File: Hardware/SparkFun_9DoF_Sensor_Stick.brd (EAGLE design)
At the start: 34.3 x 10.2 mm, 32 parts, among them U1 ITG-32001:1, U2 ADXL345", U3 3.3V/150mA, U4 HMC5883LSMD

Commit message: Updating for QC checks
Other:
- board text added: "PCB Thickness: 0.036 inches"
- board text added: "PWR"
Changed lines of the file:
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@@
 <setting verticaltext="up"/>
 </settings>
-<grid distance="0.01" unitdist="inch" unit="inch" style="lines" multiple="1" display="yes" altdistance="0.005" altunitdist="inch" altunit="inch"/>
+<grid distance="0.02" unitdist="inch" unit="inch" style="lines" multiple="1" display="yes" altdistance="0.005" altunitdist="inch" altunit="inch"/>
 <layers>
 <layer number="1" name="Top" color="4" fill="1" visible="yes" active="yes"/>
@@
 <layer number="45" name="Holes" color="7" fill="1" visible="yes" active="yes"/>
 <layer number="46" name="Milling" color="3" fill="1" visible="no" active="yes"/>
-<layer number="47" name="Measures" color="7" fill="1" visible="yes" active="yes"/>
+<layer number="47" name="Measures" color="7" fill="1" visible="no" active="yes"/>
 <layer number="48" name="Document" color="7" fill="1" visible="no" active="yes"/>
 <layer number="49" name="Reference" color="7" fill="1" visible="yes" active="yes"/>
@@
 <text x="18.288" y="6.35" size="0.8128" layer="22" font="vector" ratio="15" rot="MR0">GYRO</text>
 <text x="7.874" y="11.176" size="1.778" layer="47" font="vector" ratio="15">Units in inches</text>
+<text x="7.62" y="13.97" size="1.778" layer="51" font="vector" ratio="15">PCB Thickness: 0.036 inches</text>
+<text x="7.239" y="6.477" size="0.8128" layer="21" font="vector" ratio="15" rot="R90">PWR</text>
 </plain>
 <attributes>

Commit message: Changes from engineering review
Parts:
- removed SJ2: JUMPER-PAD-2-NC_BY_TRACE, SparkFun-Passives:PAD-JUMPER-2-NC_BY_TRACE_YES_SILK
- added R4, R5: DNP, SparkFun-Resistors:0603-RES
- added SJ5: JUMPER-PAD-3-2OF3_NC_BY_TRACE_LARGE, SparkFun-Passives:PAD-JUMPER-3-2OF3_NC_BY_TRACE_YES_SILK_LARGE
- SJ3: value JUMPER-PAD-2-NC_BY_TRACE -> JUMPER-PAD-3-2OF3_NC_BY_TRACE_LARGE; device SparkFun-Passives:PAD-JUMPER-2-NC_BY_TRACE_YES_SILK -> SparkFun-Passives:PAD-JUMPER-3-2OF3_NC_BY_TRACE_YES_SILK_LARGE
- moved U$3 1.15 mm to (7.33, 1.62)
- moved SJ3 0.76 mm to (17.9, 5.08)
- moved R3 0.13 mm to (8.74, 8.51)
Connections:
- new net N$11: R4.1, SJ3.1
- new net N$13: R5.1, SJ5.1
- net 3.3V: now also R4.2, R5.2
- net GND: now also SJ3.3, SJ5.3; no longer SJ2.1, SJ3.1
- net N$10: now also SJ5.2; no longer SJ2.2
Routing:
- net SCL: track 48.2 -> 42.0 mm
- net 3.3V: track 67.8 -> 71.6 mm, vias 5 -> 7
- net N$10: track 5.16 -> 8.01 mm
- net SDA: track 40.5 -> 42.9 mm
- net N$9: track 3.89 -> 5.76 mm
- net N$13: track 0.00 -> 1.54 mm
- net N$11: track 0.00 -> 1.54 mm
- net GND: track 17.4 -> 18.1 mm
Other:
- board text added: "GYRO ADD."
- board text added: "MAG."
- board text removed: "MAGNETO"

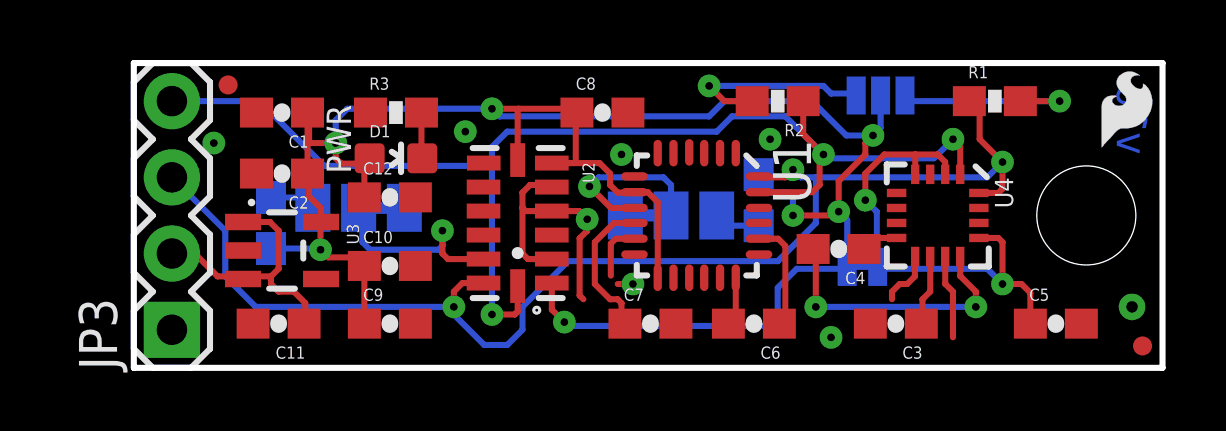
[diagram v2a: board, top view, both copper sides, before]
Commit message: Fixing QC issues
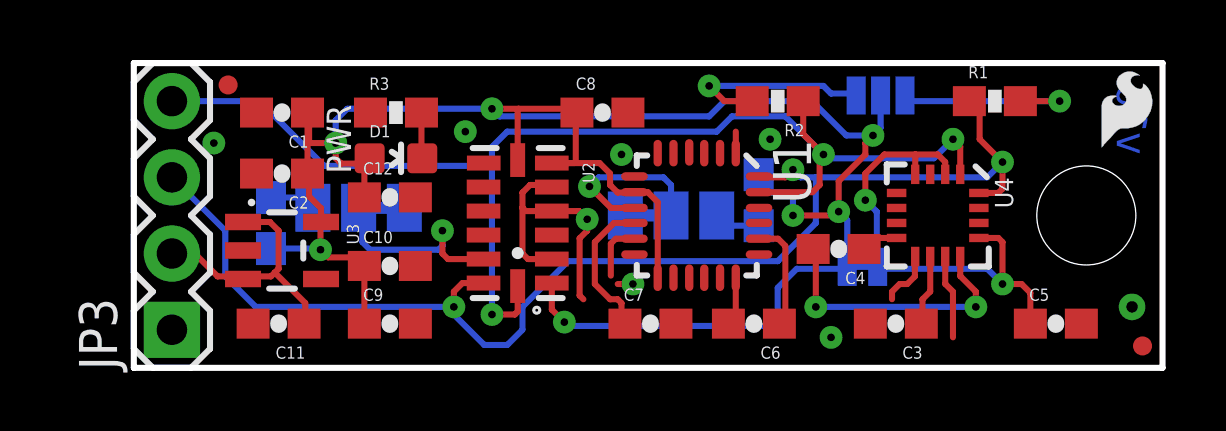
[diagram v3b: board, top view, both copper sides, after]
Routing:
- net GND: track 18.1 -> 18.8 mm
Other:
- board text added: "ADDR"
- board text added: "GYRO ADDR"
- board text removed: "ACL"
- board text removed: "ADD."
- board text removed: "GYRO ADD."
- board text removed: "MAG."
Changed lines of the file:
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@@
 <setting verticaltext="up"/>
 </settings>
-<grid distance="0.05" unitdist="inch" unit="inch" style="lines" multiple="1" display="yes" altdistance="0.005" altunitdist="inch" altunit="inch"/>
+<grid distance="0.005" unitdist="inch" unit="inch" style="lines" multiple="1" display="yes" altdistance="0.005" altunitdist="inch" altunit="inch"/>
 <layers>
 <layer number="1" name="Top" color="4" fill="1" visible="yes" active="yes"/>
@@
 <circle x="12.03325" y="2.88925" radius="0.635" width="0.2032" layer="22"/>
 <circle x="31.75" y="5.08" radius="1.27" width="0.254" layer="49"/>
-<text x="4.699" y="0.889" size="0.8128" layer="22" font="vector" ratio="15" rot="MR0">GND</text>
-<text x="4.699" y="3.429" size="0.8128" layer="22" font="vector" ratio="15" rot="MR0">VCC</text>
-<text x="4.699" y="5.969" size="0.8128" layer="22" font="vector" ratio="15" rot="MR0">SDA</text>
-<text x="4.445" y="8.509" size="0.8128" layer="22" font="vector" ratio="15" rot="MR0">SCL</text>
+<text x="3.429" y="2.413" size="0.8128" layer="22" font="vector" ratio="15" rot="MR270">GND</text>
+<text x="3.429" y="4.953" size="0.8128" layer="22" font="vector" ratio="15" rot="MR270">VCC</text>
+<text x="3.429" y="7.493" size="0.8128" layer="22" font="vector" ratio="15" rot="MR270">SDA</text>
+<text x="3.429" y="10.033" size="0.8128" layer="22" font="vector" ratio="15" rot="MR270">SCL</text>
 <text x="17.526" y="8.41375" size="1.4224" layer="22" font="vector" ratio="15" rot="MR0">9DOF Stick</text>
 <text x="13.68425" y="0.73025" size="1.016" layer="22" font="vector" ratio="15" rot="MR0">X</text>
@@
 <text x="14.57325" y="5.17525" size="1.016" layer="22" font="vector" ratio="15" rot="MR0">ACCEL</text>
 <text x="20.09775" y="0.254" size="1.016" layer="22" font="vector" ratio="15" rot="MR90">GYRO</text>
-<text x="29.2735" y="4.5085" size="1.016" layer="22" font="vector" ratio="15" rot="MR0">MAG.</text>
+<text x="29.2735" y="4.5085" size="1.016" layer="22" font="vector" ratio="15" rot="MR0">MAG</text>
 <text x="26.67" y="-12.7" size="1.778" layer="51" font="vector" ratio="15">C. Taylor and N. Seidle</text>
 <text x="32.766" y="7.112" size="1.016" layer="16" font="vector" ratio="20" rot="MR90">v16</text>
@@
 <text x="23.114" y="8.636" size="0.8128" layer="22" font="vector" ratio="15" rot="MR0">P/U</text>
 <text x="25.273" y="4.572" size="0.8128" layer="22" font="vector" ratio="15" rot="MR0">MAG</text>
-<text x="25.4" y="1.397" size="0.8128" layer="22" font="vector" ratio="15" rot="MR0">ADD.</text>
-<text x="8.636" y="3.302" size="0.8128" layer="22" font="vector" ratio="15" rot="MR0">ADD.</text>
-<text x="8.636" y="6.477" size="0.8128" layer="22" font="vector" ratio="15" rot="MR0">ACL</text>
-<text x="21.082" y="6.223" size="0.8128" layer="22" font="vector" ratio="15" rot="MR0">GYRO ADD.</text>
+<text x="25.654" y="1.397" size="0.8128" layer="22" font="vector" ratio="15" rot="MR0">ADDR</text>
+<text x="9.398" y="3.302" size="0.8128" layer="22" font="vector" ratio="15" rot="MR0">ADDR</text>
+<text x="9.398" y="6.477" size="0.8128" layer="22" font="vector" ratio="15" rot="MR0">ACCEL</text>
+<text x="19.304" y="6.223" size="0.8128" layer="22" font="vector" ratio="15" rot="MR0">GYRO
+ADDR</text>
 <text x="6.223" y="-6.223" size="1.778" layer="47" font="vector" ratio="15">Units in inches</text>
 <text x="-2.54" y="13.335" size="1.778" layer="51" font="vector" ratio="15">PCB Thickness: 0.036 inches</text>
@@
 <wire x1="15.113" y1="4.953" x2="15.113" y2="4.572" width="0.2032" layer="1"/>
 <wire x1="15.113" y1="4.572" x2="14.859" y2="4.318" width="0.2032" layer="1"/>
+<wire x1="20.066" y1="7.493" x2="20.066" y2="7.874" width="0.2032" layer="1"/>
+<wire x1="20.06505" y1="7.1562" x2="20.06505" y2="7.49205" width="0.2032" layer="1"/>
+<wire x1="20.06505" y1="7.49205" x2="20.066" y2="7.493" width="0.2032" layer="1"/>
 </signal>
 <signal name="SDA">
@@
 <wire x1="4.5364" y1="4.8616" x2="4.826" y2="4.572" width="0.2032" layer="1"/>
 <wire x1="4.826" y1="4.572" x2="4.826" y2="3.302" width="0.2032" layer="1"/>
-<wire x1="4.826" y1="3.302" x2="4.572" y2="3.048" width="0.2032" layer="1"/>
+<wire x1="4.826" y1="3.302" x2="4.699" y2="3.175" width="0.2032" layer="1"/>
+<wire x1="4.699" y1="3.175" x2="4.572" y2="3.048" width="0.2032" layer="1"/>
 <wire x1="4.572" y1="3.048" x2="3.7266" y2="3.048" width="0.2032" layer="1"/>
 <wire x1="3.7266" y1="3.048" x2="3.6402" y2="2.9616" width="0.2032" layer="1"/>
-<wire x1="4.572" y1="3.048" x2="4.572" y2="2.794" width="0.2032" layer="1"/>
 <wire x1="5.715" y1="2.159" x2="5.715" y2="1.5122" width="0.2032" layer="1"/>
 <wire x1="5.715" y1="1.5122" x2="5.676" y2="1.4732" width="0.2032" layer="1"/>
-<wire x1="5.715" y1="2.159" x2="5.334" y2="2.54" width="0.2032" layer="1"/>
-<wire x1="5.334" y1="2.54" x2="4.826" y2="2.54" width="0.2032" layer="1"/>
-<wire x1="4.826" y1="2.54" x2="4.572" y2="2.794" width="0.2032" layer="1"/>
+<wire x1="5.715" y1="2.159" x2="4.699" y2="3.175" width="0.2032" layer="1"/>
 </signal>
 <signal name="N$4">
@@
 </board>
 </drawing>
+<compatibility>
+<note version="6.3" minversion="6.2.2" severity="warning">
+Since Version 6.2.2 text objects can contain more than one line,
+which will not be processed correctly with this version.
+</note>
+</compatibility>
 </eagle>

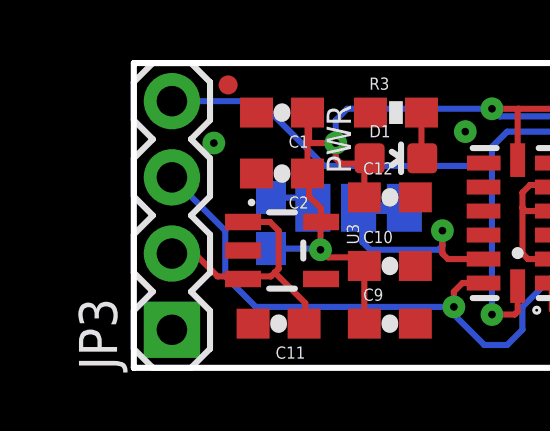
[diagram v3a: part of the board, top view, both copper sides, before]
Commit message: Swapping JP1 and JP3 names on parts
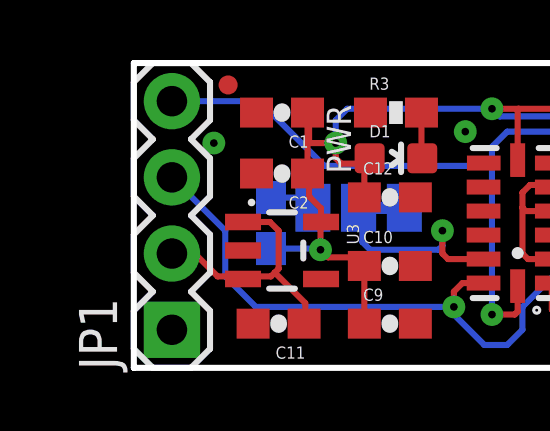
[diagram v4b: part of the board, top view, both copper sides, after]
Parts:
- JP1: value FIDUCIALUFIDUCIAL -> (none); device SparkFun-Aesthetics:MICRO-FIDUCIAL -> SparkFun-Connectors:1X04
- JP3: value (none) -> FIDUCIALUFIDUCIAL; device SparkFun-Connectors:1X04 -> SparkFun-Aesthetics:MICRO-FIDUCIAL
- moved JP1 8.37 mm to (1.27, 1.27), turned to 90 degrees
- moved JP3 8.37 mm to (3.14, 9.43), turned to 0 degrees
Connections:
- net GND: now also JP1.1; no longer JP3.1
- net SCL: now also JP1.4; no longer JP3.4
- net SDA: now also JP1.3; no longer JP3.3
- net VCC: now also JP1.2; no longer JP3.2
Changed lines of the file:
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@@
 <setting verticaltext="up"/>
 </settings>
-<grid distance="0.005" unitdist="inch" unit="inch" style="lines" multiple="1" display="yes" altdistance="0.005" altunitdist="inch" altunit="inch"/>
+<grid distance="0.05" unitdist="inch" unit="inch" style="lines" multiple="1" display="yes" altdistance="0.005" altunitdist="inch" altunit="inch"/>
 <layers>
 <layer number="1" name="Top" color="4" fill="1" visible="yes" active="yes"/>
@@
 <layer number="47" name="Measures" color="7" fill="1" visible="no" active="yes"/>
 <layer number="48" name="Document" color="7" fill="1" visible="no" active="yes"/>
-<layer number="49" name="Reference" color="7" fill="1" visible="yes" active="yes"/>
+<layer number="49" name="Reference" color="7" fill="1" visible="no" active="yes"/>
 <layer number="50" name="dxf" color="7" fill="1" visible="no" active="yes"/>
 <layer number="51" name="tDocu" color="6" fill="1" visible="yes" active="yes"/>
@@
 <attribute name="VALUE" value="0.1uF" x="8.5344" y="1.4732" size="1.778" layer="27" display="off"/>
 </element>
-<element name="JP3" library="SparkFun-Connectors" package="1X04" value="" x="1.27" y="1.27" rot="R90"/>
+<element name="JP1" library="SparkFun-Connectors" package="1X04" value="" x="1.27" y="1.27" rot="R90"/>
 <element name="C10" library="SparkFun-Capacitors" package="0603-CAP" value="0.1uF" x="8.5344" y="3.39725">
 <attribute name="PROD_ID" value="CAP-00810" x="8.5344" y="3.39725" size="1.778" layer="27" display="off"/>
@@
 <attribute name="VALUE" value="330" x="8.7376" y="8.509" size="1.778" layer="27" display="off"/>
 </element>
-<element name="JP1" library="SparkFun-Aesthetics" package="MICRO-FIDUCIAL" value="FIDUCIALUFIDUCIAL" x="3.14325" y="9.42975"/>
+<element name="JP3" library="SparkFun-Aesthetics" package="MICRO-FIDUCIAL" value="FIDUCIALUFIDUCIAL" x="3.14325" y="9.42975"/>
 <element name="JP2" library="SparkFun-Aesthetics" package="MICRO-FIDUCIAL" value="FIDUCIALUFIDUCIAL" x="33.62325" y="0.73025"/>
 <element name="U4" library="SparkFun-Sensors" package="16LPCC" value="HMC5883LSMD" x="26.797" y="5.08" rot="R270">
@@
 </polygon>
 <contactref element="U3" pad="2"/>
-<contactref element="JP3" pad="1"/>
+<contactref element="JP1" pad="1"/>
 <contactref element="C12" pad="2"/>
 <wire x1="25.273" y1="2.286" x2="25.273" y2="2.54" width="0.2032" layer="1"/>
@@
 <contactref element="R1" pad="1"/>
 <contactref element="U4" pad="16"/>
-<contactref element="JP3" pad="3"/>
+<contactref element="JP1" pad="3"/>
 <via x="10.668" y="2.032" extent="1-16" drill="0.254"/>
 <wire x1="10.668" y1="2.032" x2="10.668" y2="1.778" width="0.2032" layer="16"/>
@@
 <contactref element="R2" pad="1"/>
 <contactref element="U4" pad="1"/>
-<contactref element="JP3" pad="4"/>
+<contactref element="JP1" pad="4"/>
 <via x="11.938" y="1.778" extent="1-16" drill="0.254"/>
 <via x="27.305" y="7.62" extent="1-16" drill="0.254"/>
@@
 <contactref element="U3" pad="1"/>
 <contactref element="U3" pad="3"/>
-<contactref element="JP3" pad="2"/>
+<contactref element="JP1" pad="2"/>
 <wire x1="1.27" y1="3.81" x2="2.032" y2="3.81" width="0.2032" layer="1"/>
 <wire x1="2.032" y1="3.81" x2="2.794" y2="3.048" width="0.2032" layer="1"/>
